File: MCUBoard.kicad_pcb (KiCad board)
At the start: 2 copper layers, 90 x 90 mm, 62 parts, among them J1 USB_B_Micro, J10 Conn_01x04, J2 Conn_01x04, J3 Conn_02x03_Odd_Even, J4 Conn_02x05_Odd_Even, J5 Conn_01x04, J6 Conn_01x04, J7 Conn_01x16, J8 Conn_01x18, J9 Conn_01x04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

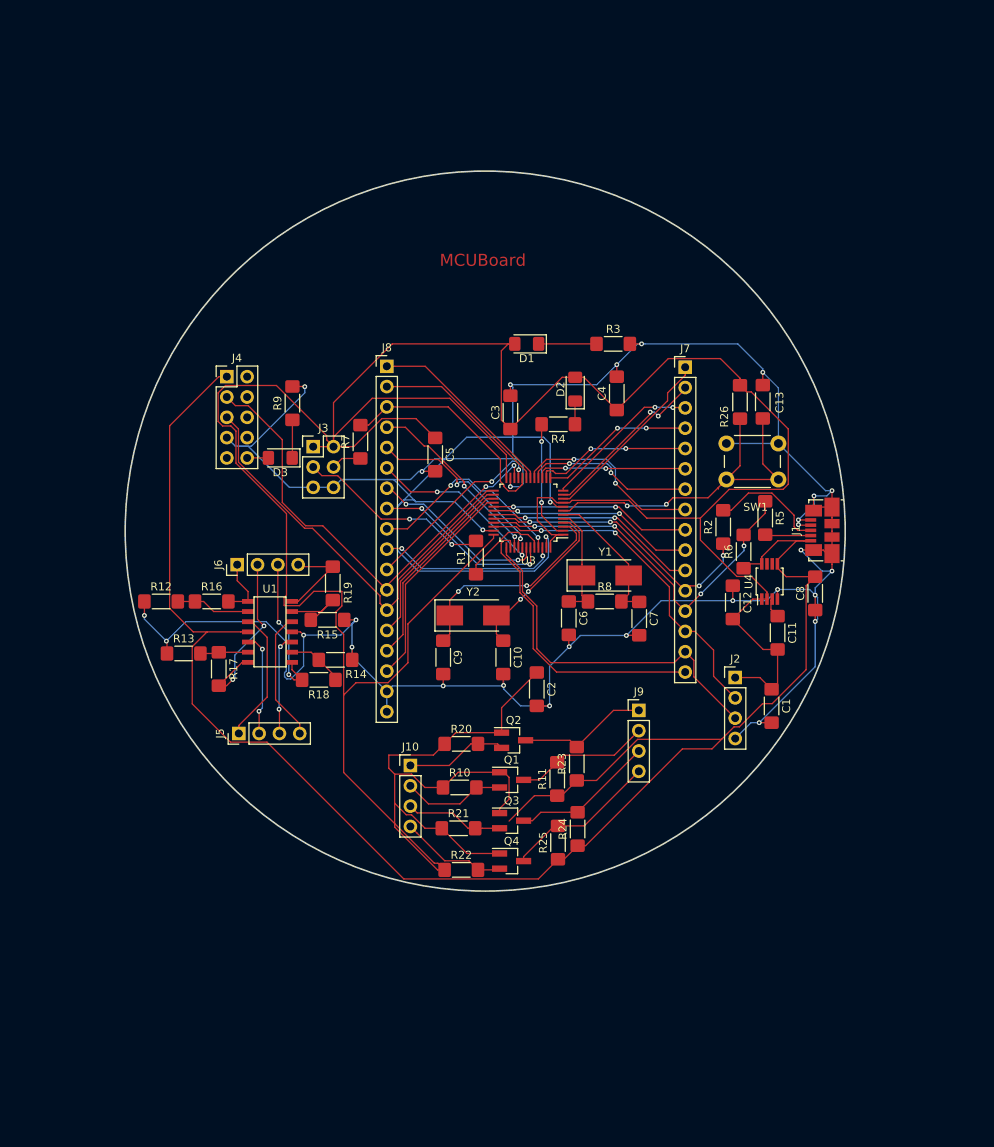
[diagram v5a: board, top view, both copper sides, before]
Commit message: copper fill added
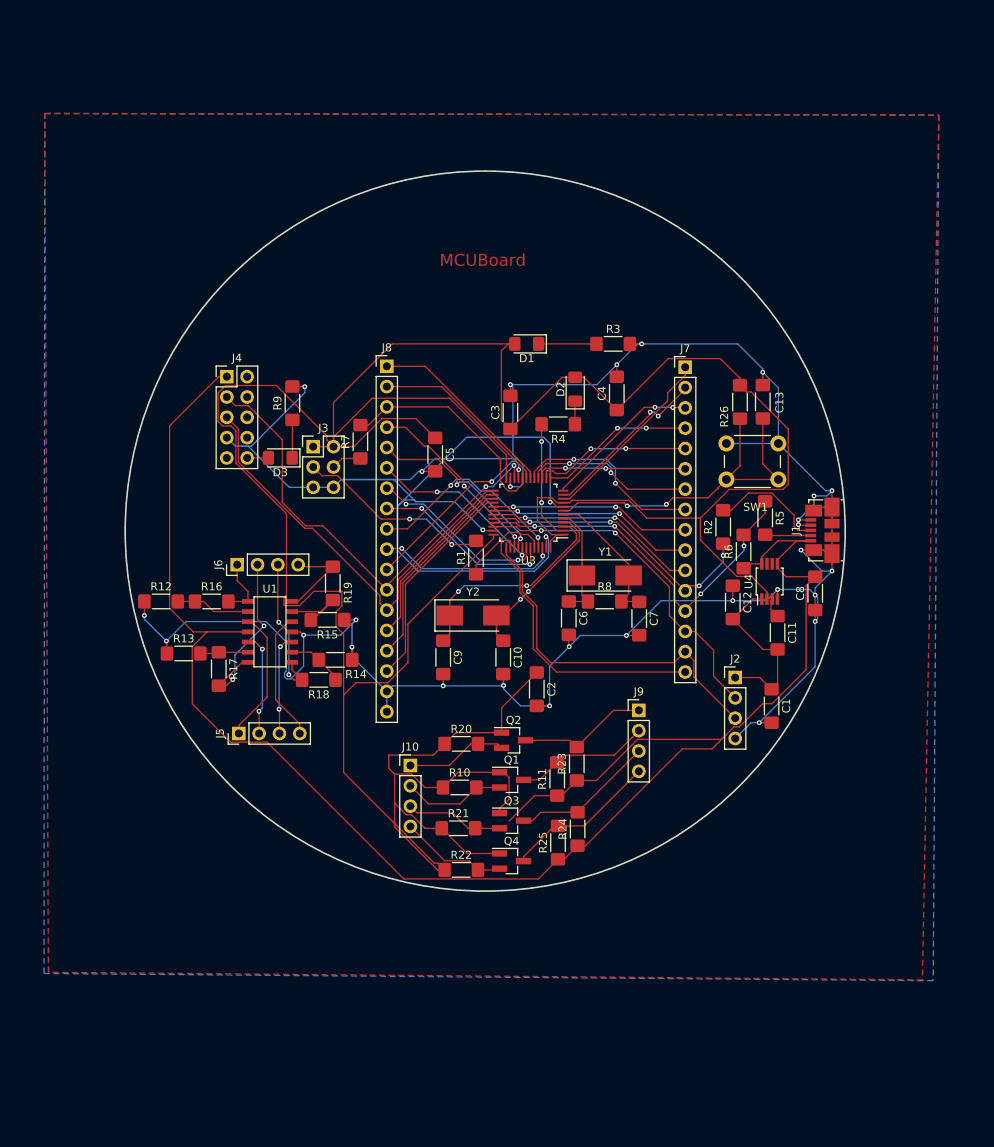
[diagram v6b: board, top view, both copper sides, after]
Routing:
- added copper zone on F.Cu, net +3V3
- added copper zone on B.Cu, net GND
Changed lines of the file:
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@@
   (segment (start 129.515 110.06) (end 130.95 108.625) (width 0.155) (layer F.Cu) (net 76))
   (segment (start 125.85 110.06) (end 129.515 110.06) (width 0.155) (layer F.Cu) (net 76))
+  (zone (net 1) (net_name +3V3) (layer F.Cu) (hatch edge 0.508)
+    (connect_pads (clearance 0.508))
+    (min_thickness 0.254)
+    (fill yes (arc_segments 16) (thermal_gap 0.508) (thermal_bridge_width 0.508))
+    (polygon
+      (pts
+        (xy 94.95 47.8) (xy 206.7 48) (xy 204.65 156.1) (xy 95.4 155.15)
+      )
+    )
+  )
+  (zone (net 2) (net_name GND) (layer B.Cu) (hatch edge 0.508)
+    (connect_pads (clearance 0.508))
+    (min_thickness 0.254)
+    (fill yes (arc_segments 16) (thermal_gap 0.508) (thermal_bridge_width 0.508))
+    (polygon
+      (pts
+        (xy 94.95 47.8) (xy 206.7 48) (xy 206 156.2) (xy 94.85 155.3)
+      )
+    )
+  )
 )
